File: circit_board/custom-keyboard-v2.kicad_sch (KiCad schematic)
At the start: 139 parts, among them SW1 SW_Push, SW10 SW_Push, SW11 SW_Push, SW12 SW_Push, SW13 SW_Push, SW14 SW_Push, SW15 SW_Push, SW16 SW_Push, SW17 SW_Push, SW18 SW_Push, SW19 SW_Push, SW2 SW_Push, SW20 SW_Push, SW21 SW_Push, SW22 SW_Push, SW23 SW_Push, SW24 SW_Push, SW25 SW_Push, SW26 SW_Push, SW27 SW_Push, SW28 SW_Push, SW29 SW_Push, SW3 SW_Push, SW30 SW_Push, SW31 SW_Push, SW32 SW_Push, SW33 SW_Push, SW34 SW_Push, SW35 SW_Push, SW36 SW_Push, SW37 SW_Push, SW38 SW_Push, SW39 SW_Push, SW4 SW_Push, SW40 SW_Push, SW41 SW_Push, SW42 SW_Push, SW43 SW_Push, SW44 SW_Push, SW45 SW_Push, SW46 SW_Push, SW5 SW_Push, SW6 SW_Push, SW7 SW_Push, SW8 SW_Push, SW9 SW_Push

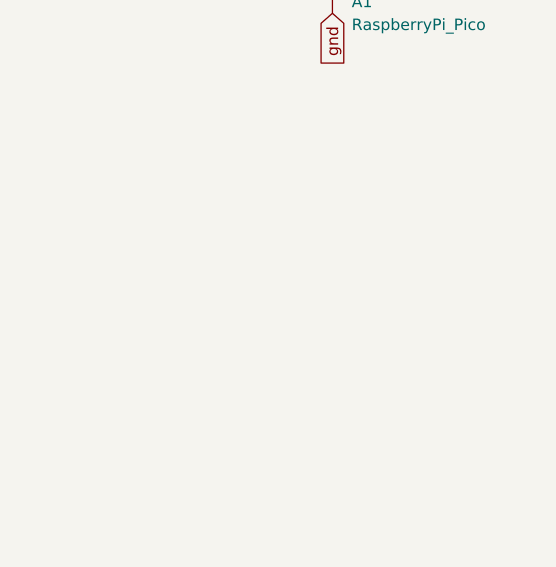
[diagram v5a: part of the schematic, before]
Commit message: Added vertical offset to keys
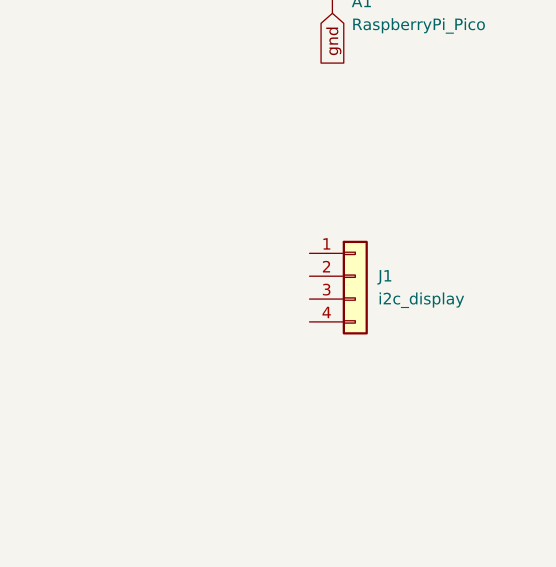
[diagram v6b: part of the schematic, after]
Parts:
- added J1: i2c_display, symbol Connector_Generic:Conn_01x04
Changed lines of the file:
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@@
+	)
+	(symbol
+		(lib_id "Connector_Generic:Conn_01x04")
+		(at 364.49 137.16 0)
+		(unit 1)
+		(exclude_from_sim no)
+		(in_bom yes)
+		(on_board yes)
+		(dnp no)
+		(fields_autoplaced yes)
+		(property "Reference" "J1"
+			(at 367.03 137.1599 0)
+			(effects
+				(font
+					(size 1.27 1.27)
+				)
+				(justify left)
+			)
+		)
+		(property "Value" "i2c_display"
+			(at 367.03 139.6999 0)
+			(effects
+				(font
+					(size 1.27 1.27)
+				)
+				(justify left)
+			)
+		)
+		(property "Footprint" ""
+			(at 364.49 137.16 0)
+			(effects
+				(font
+					(size 1.27 1.27)
+				)
+				(hide yes)
+			)
+		)
+		(property "Datasheet" "~"
+			(at 364.49 137.16 0)
+			(effects
+				(font
+					(size 1.27 1.27)
+				)
+				(hide yes)
+			)
+		)
+		(property "Description" "Generic connector, single row, 01x04, script generated (kicad-library-utils/schlib/autogen/connector/)"
+			(at 364.49 137.16 0)
+			(effects
+				(font
+					(size 1.27 1.27)
+				)
+				(hide yes)
+			)
+		)
+		(pin "1"
+		)
+		(pin "3"
+		)
+		(pin "2"
+		)
+		(pin "4"
+		)
+		(instances
+			(project ""
+				(path "/36474163-3bb3-437a-8dcc-c4f15d3a343c"
+					(reference "J1")
+					(unit 1)
+				)
+			)
+		)
 	)
 	(symbol

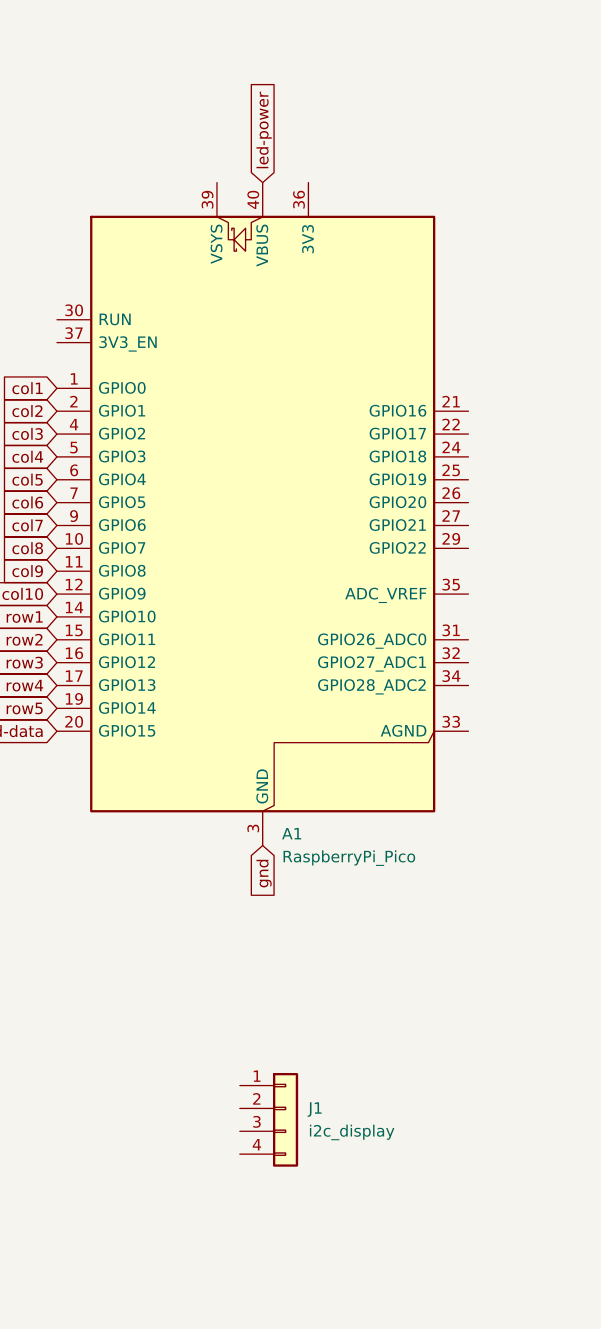
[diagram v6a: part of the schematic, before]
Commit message: Added I2C OLED display
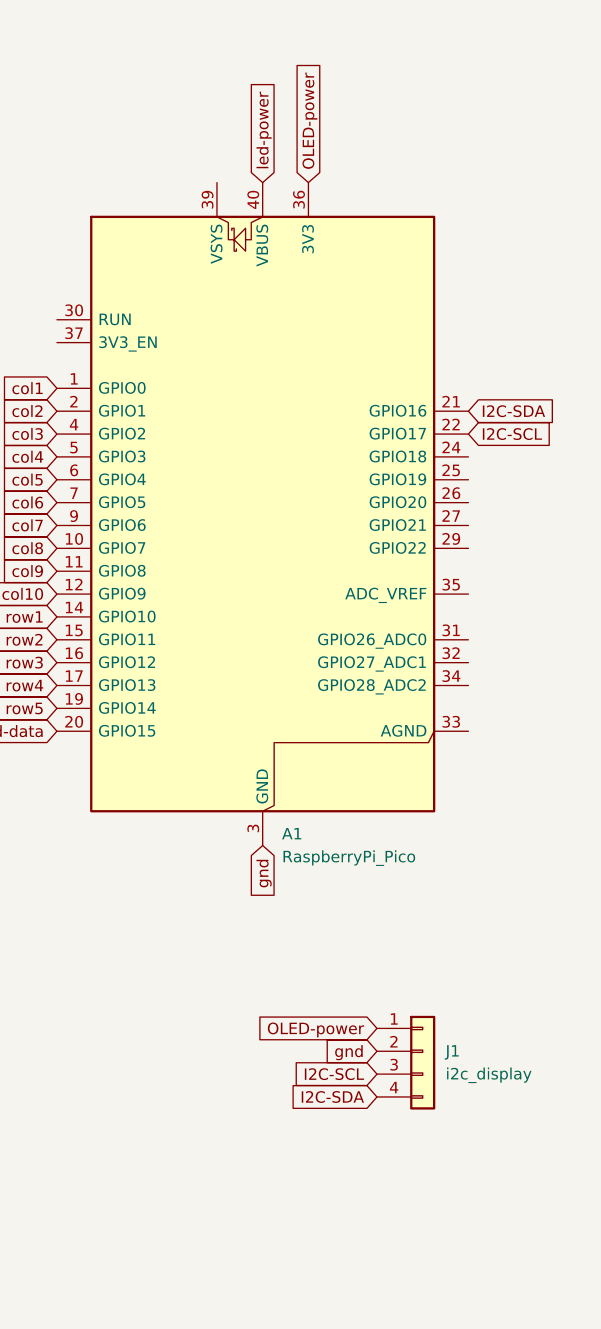
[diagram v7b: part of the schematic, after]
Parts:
- J1: footprint (none) -> Connector_PinHeader_2.54mm:PinHeader_1x04_P2.54mm_Vertical
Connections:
- net gnd: now also J1.2 (Pin_2)
- net I2C-SDA: now reaches A1.21 (GPIO16)
- net I2C-SDA: now also J1.4 (Pin_4)
- net I2C-SCL: now reaches A1.22 (GPIO17)
- net I2C-SCL: now also J1.3 (Pin_3)
- net OLED-power: now reaches A1.36 (3V3)
- net OLED-power: now also J1.1 (Pin_1)
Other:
- moved on the sheet: J1
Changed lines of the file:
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@@
 		)
 	)
+	(global_label "I2C-SCL"
+		(shape input)
+		(at 374.65 133.35 180)
+		(fields_autoplaced yes)
+		(effects
+			(font
+				(size 1.27 1.27)
+			)
+			(justify right)
+		)
+		(property "Intersheetrefs" "${INTERSHEET_REFS}"
+			(at 363.5005 133.35 0)
+			(effects
+				(font
+					(size 1.27 1.27)
+				)
+				(justify right)
+				(hide yes)
+			)
+		)
+	)
+	(global_label "I2C-SDA"
+		(shape input)
+		(at 384.81 59.69 0)
+		(fields_autoplaced yes)
+		(effects
+			(font
+				(size 1.27 1.27)
+			)
+			(justify left)
+		)
+		(property "Intersheetrefs" "${INTERSHEET_REFS}"
+			(at 396.02 59.69 0)
+			(effects
+				(font
+					(size 1.27 1.27)
+				)
+				(justify left)
+				(hide yes)
+			)
+		)
+	)
 	(global_label "col6"
 		(shape input)
@@
 		)
 	)
+	(global_label "gnd"
+		(shape input)
+		(at 374.65 130.81 180)
+		(fields_autoplaced yes)
+		(effects
+			(font
+				(size 1.27 1.27)
+			)
+			(justify right)
+		)
+		(property "Intersheetrefs" "${INTERSHEET_REFS}"
+			(at 368.2178 130.81 0)
+			(effects
+				(font
+					(size 1.27 1.27)
+				)
+				(justify right)
+				(hide yes)
+			)
+		)
+	)
 	(global_label "row2"
 		(shape input)
@@
 		)
 	)
+	(global_label "OLED-power"
+		(shape input)
+		(at 367.03 34.29 90)
+		(fields_autoplaced yes)
+		(effects
+			(font
+				(size 1.27 1.27)
+			)
+			(justify left)
+		)
+		(property "Intersheetrefs" "${INTERSHEET_REFS}"
+			(at 367.03 19.4515 90)
+			(effects
+				(font
+					(size 1.27 1.27)
+				)
+				(justify left)
+				(hide yes)
+			)
+		)
+	)
 	(global_label "col6"
 		(shape input)
@@
 		)
 	)
+	(global_label "I2C-SCL"
+		(shape input)
+		(at 384.81 62.23 0)
+		(fields_autoplaced yes)
+		(effects
+			(font
+				(size 1.27 1.27)
+			)
+			(justify left)
+		)
+		(property "Intersheetrefs" "${INTERSHEET_REFS}"
+			(at 395.9595 62.23 0)
+			(effects
+				(font
+					(size 1.27 1.27)
+				)
+				(justify left)
+				(hide yes)
+			)
+		)
+	)
 	(global_label "row5"
 		(shape input)
@@
 		)
 	)
+	(global_label "OLED-power"
+		(shape input)
+		(at 374.65 128.27 180)
+		(fields_autoplaced yes)
+		(effects
+			(font
+				(size 1.27 1.27)
+			)
+			(justify right)
+		)
+		(property "Intersheetrefs" "${INTERSHEET_REFS}"
+			(at 359.8115 128.27 0)
+			(effects
+				(font
+					(size 1.27 1.27)
+				)
+				(justify right)
+				(hide yes)
+			)
+		)
+	)
+	(global_label "I2C-SDA"
+		(shape input)
+		(at 374.65 135.89 180)
+		(fields_autoplaced yes)
+		(effects
+			(font
+				(size 1.27 1.27)
+			)
+			(justify right)
+		)
+		(property "Intersheetrefs" "${INTERSHEET_REFS}"
+			(at 363.44 135.89 0)
+			(effects
+				(font
+					(size 1.27 1.27)
+				)
+				(justify right)
+				(hide yes)
+			)
+		)
+	)
 	(global_label "col9"
 		(shape input)
@@
 	(symbol
 		(lib_id "Connector_Generic:Conn_01x04")
-		(at 364.49 137.16 0)
+		(at 379.73 130.81 0)
 		(unit 1)
 		(exclude_from_sim no)
@@
 		(fields_autoplaced yes)
 		(property "Reference" "J1"
-			(at 367.03 137.1599 0)
+			(at 382.27 130.8099 0)
 			(effects
 				(font
@@
 		)
 		(property "Value" "i2c_display"
-			(at 367.03 139.6999 0)
+			(at 382.27 133.3499 0)
 			(effects
 				(font
@@
 			)
 		)
-		(property "Footprint" ""
-			(at 364.49 137.16 0)
+		(property "Footprint" "Connector_PinHeader_2.54mm:PinHeader_1x04_P2.54mm_Vertical"
+			(at 379.73 130.81 0)
 			(effects
 				(font
@@
 		)
 		(property "Datasheet" "~"
-			(at 364.49 137.16 0)
+			(at 379.73 130.81 0)
 			(effects
 				(font
@@
 		)
 		(property "Description" "Generic connector, single row, 01x04, script generated (kicad-library-utils/schlib/autogen/connector/)"
-			(at 364.49 137.16 0)
+			(at 379.73 130.81 0)
 			(effects
 				(font

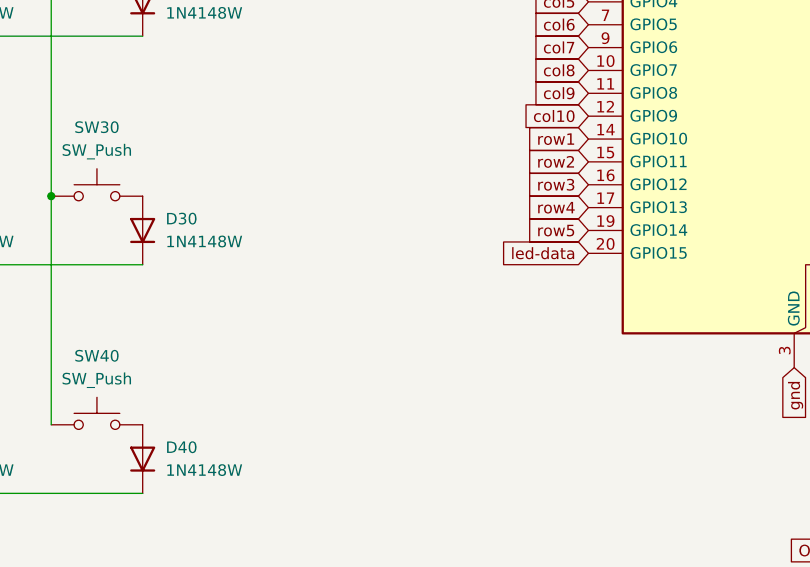
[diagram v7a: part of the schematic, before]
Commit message: Added 3V -> 5V converter for LED data line
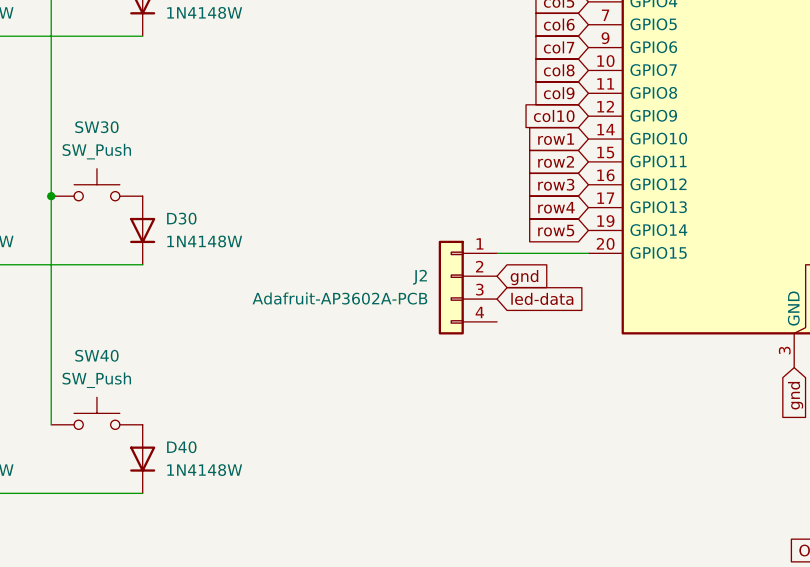
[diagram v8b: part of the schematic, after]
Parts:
- added J2: Adafruit-AP3602A-PCB, Connector_PinHeader_2.54mm:PinHeader_1x04_P2.54mm_Vertical, symbol Connector_Generic:Conn_01x04
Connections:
- net gnd: now also J2.2 (Pin_2)
- net led-data: now also J2.3 (Pin_3); no longer A1.20 (GPIO15)
- new net: A1.20 (GPIO15), J2.1 (Pin_1)
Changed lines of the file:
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@@
+	(wire
+		(pts
+			(xy 328.93 95.25) (xy 339.09 95.25)
+		)
+		(stroke
+			(width 0)
+			(type default)
+		)
+	)
 	(wire
 		(pts
@@
 		)
 	)
+	(global_label "gnd"
+		(shape input)
+		(at 328.93 97.79 0)
+		(fields_autoplaced yes)
+		(effects
+			(font
+				(size 1.27 1.27)
+			)
+			(justify left)
+		)
+		(property "Intersheetrefs" "${INTERSHEET_REFS}"
+			(at 335.3622 97.79 0)
+			(effects
+				(font
+					(size 1.27 1.27)
+				)
+				(justify left)
+				(hide yes)
+			)
+		)
+	)
 	(global_label "col3"
 		(shape input)
@@
 	(global_label "led-data"
 		(shape input)
-		(at 339.09 95.25 180)
-		(fields_autoplaced yes)
-		(effects
-			(font
-				(size 1.27 1.27)
-			)
-			(justify right)
-		)
-		(property "Intersheetrefs" "${INTERSHEET_REFS}"
-			(at 327.4569 95.25 0)
-			(effects
-				(font
-					(size 1.27 1.27)
-				)
-				(justify right)
+		(at 328.93 100.33 0)
+		(fields_autoplaced yes)
+		(effects
+			(font
+				(size 1.27 1.27)
+			)
+			(justify left)
+		)
+		(property "Intersheetrefs" "${INTERSHEET_REFS}"
+			(at 340.5631 100.33 0)
+			(effects
+				(font
+					(size 1.27 1.27)
+				)
+				(justify left)
 				(hide yes)
 			)
@@
 					(unit 1)
 				)
+			)
+		)
+	)
+	(symbol
+		(lib_id "Connector_Generic:Conn_01x04")
+		(at 323.85 97.79 0)
+		(mirror y)
+		(unit 1)
+		(exclude_from_sim no)
+		(in_bom yes)
+		(on_board yes)
+		(dnp no)
+		(property "Reference" "J2"
+			(at 321.31 97.7899 0)
+			(effects
+				(font
+					(size 1.27 1.27)
+				)
+				(justify left)
+			)
+		)
+		(property "Value" "Adafruit-AP3602A-PCB"
+			(at 321.31 100.3299 0)
+			(effects
+				(font
+					(size 1.27 1.27)
+				)
+				(justify left)
+			)
+		)
+		(property "Footprint" "Connector_PinHeader_2.54mm:PinHeader_1x04_P2.54mm_Vertical"
+			(at 323.85 97.79 0)
+			(effects
+				(font
+					(size 1.27 1.27)
+				)
+				(hide yes)
+			)
+		)
+		(property "Datasheet" "~"
+			(at 323.85 97.79 0)
+			(effects
+				(font
+					(size 1.27 1.27)
+				)
+				(hide yes)
+			)
+		)
+		(property "Description" "Generic connector, single row, 01x04, script generated (kicad-library-utils/schlib/autogen/connector/)"
+			(at 323.85 97.79 0)
+			(effects
+				(font
+					(size 1.27 1.27)
+				)
+				(hide yes)
+			)
+		)
+		(pin "1"
+		)
+		(pin "3"
+		)
+		(pin "4"
+		)
+		(pin "2"
+		)
+		(instances
+			(project ""
+				(path "/36474163-3bb3-437a-8dcc-c4f15d3a343c"
+					(reference "J2")
+					(unit 1)
+				)
